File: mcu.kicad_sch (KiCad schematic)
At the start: 41 parts, among them J1 GPIO, J2 3v3/GND, Q1 MMBTA42, U1 STM32F103C8Tx, X1 SPI_DBG, X2 MTRBTN, X3 Bluetooth, X4 Buzzer

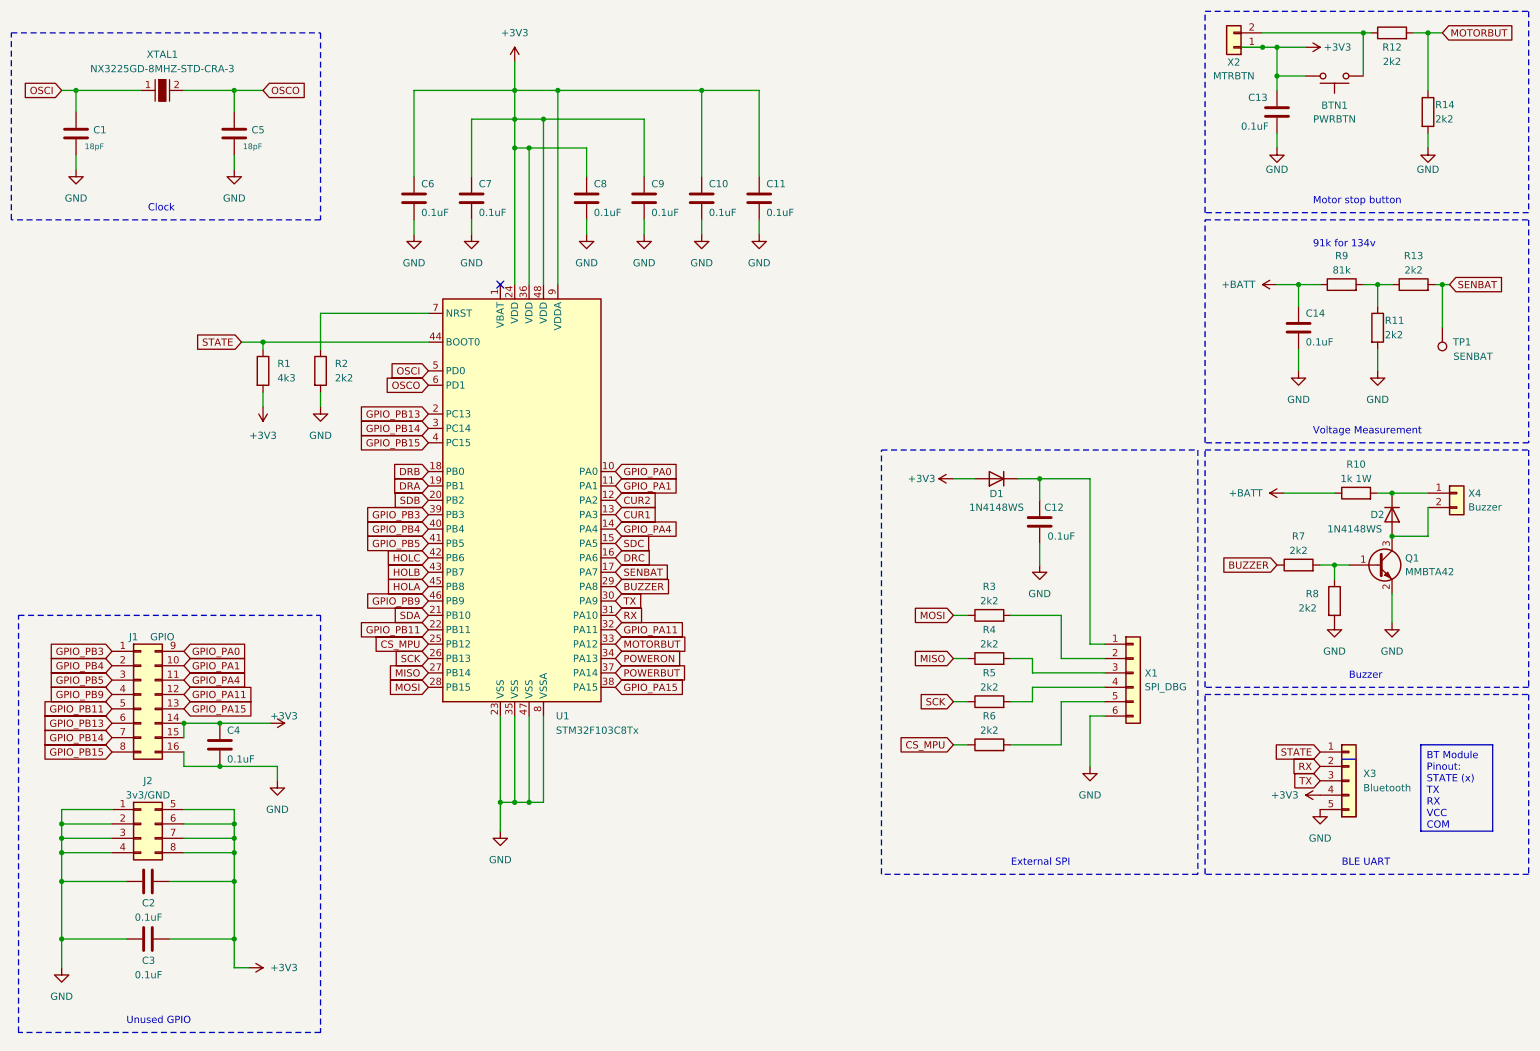
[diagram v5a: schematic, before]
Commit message: Add files via upload
Add leds and minors
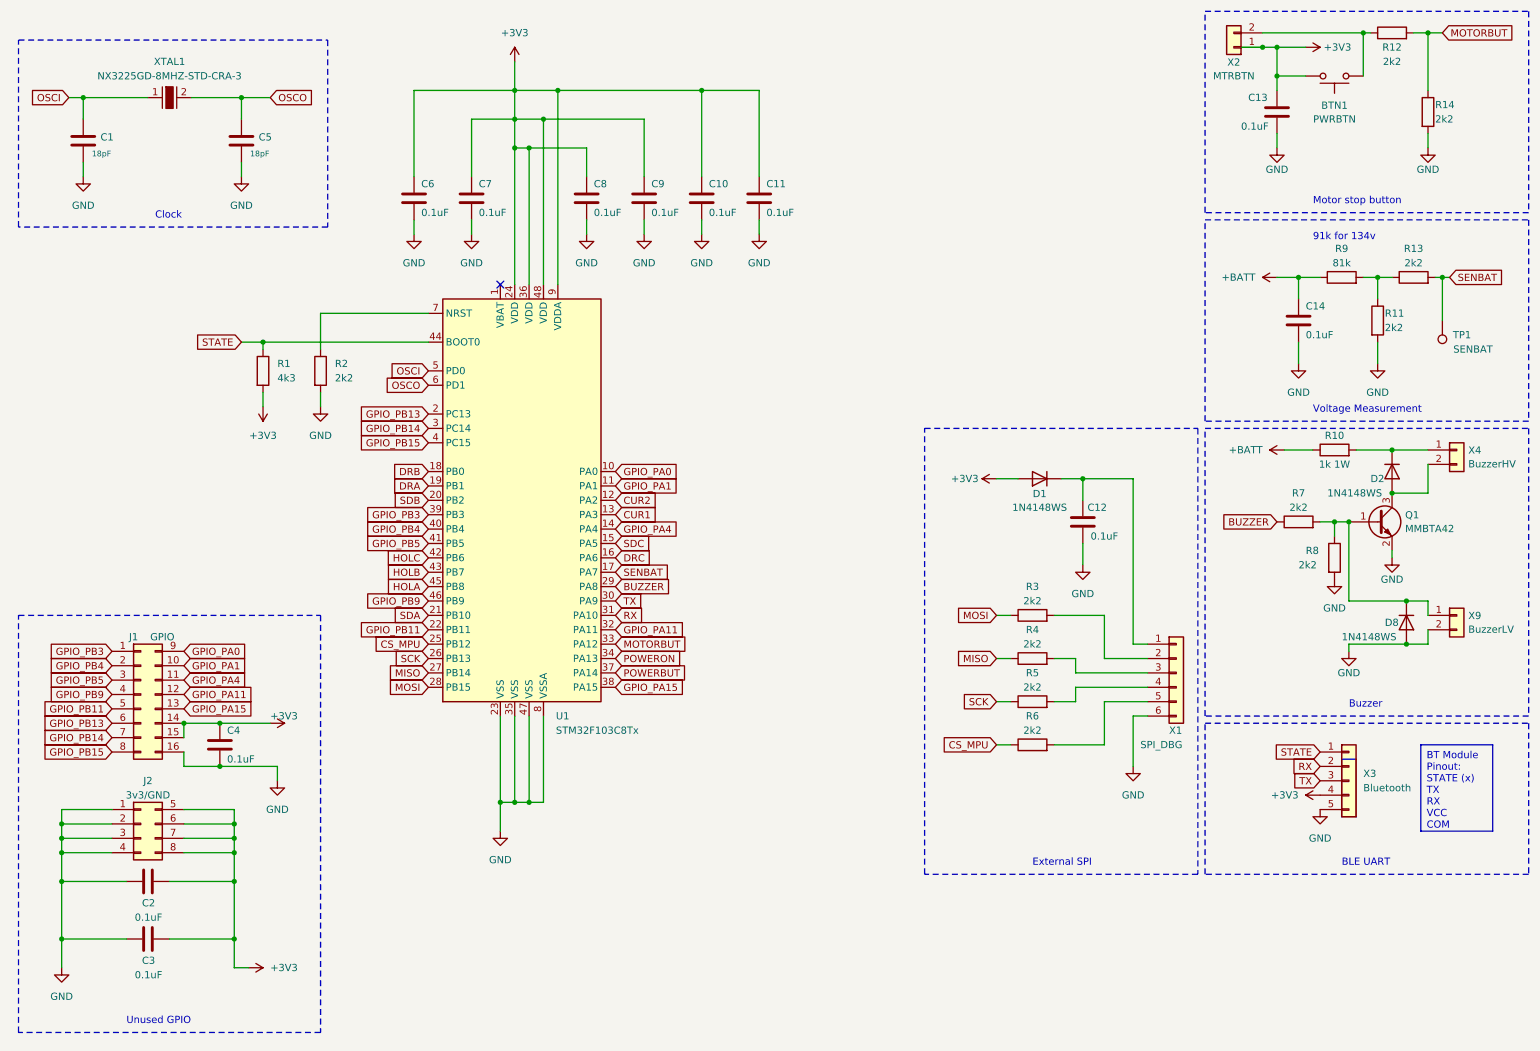
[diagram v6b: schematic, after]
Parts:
- added D8: 1N4148WS, Diode_SMD:D_SOD-323, symbol Diode:1N4148WS
- added X9: BuzzerLV, symbol Connector_Generic:Conn_01x02
- X4: value Buzzer -> BuzzerHV
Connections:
- net GND: now also D8.2 (A), X9.2 (Pin_2)
- net at Q1.1 (B), R7.2, R8.1: now also D8.1 (K), X9.1 (Pin_1)
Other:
- moved on the sheet: C1, C12, C14, C5, D1, D2, Q1, R10, R11, R13, R3, R4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

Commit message: fixed some footprints
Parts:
- J1: footprint Capacitor_SMD:CP_Elec_10x10.5 -> Connector_PinSocket_2.54mm:PinSocket_2x08_P2.54mm_Vertical
- J2: footprint Capacitor_SMD:CP_Elec_6.3x7.7 -> Connector_PinSocket_2.54mm:PinSocket_2x04_P2.54mm_Vertical
- R10: renamed from R9; value 81k -> 81k 1%; footprint Resistor_SMD:R_0603_1608Metric_Pad0.98x0.95mm_HandSolder -> Resistor_SMD:R_0805_2012Metric_Pad1.20x1.40mm_HandSolder
- R11: value 2k2 -> 2k2 1%; footprint Resistor_SMD:R_0603_1608Metric_Pad0.98x0.95mm_HandSolder -> Resistor_SMD:R_0805_2012Metric_Pad1.20x1.40mm_HandSolder
- renumbered D8 to D3, R10 to R8, R8 to R9, X9 to X5

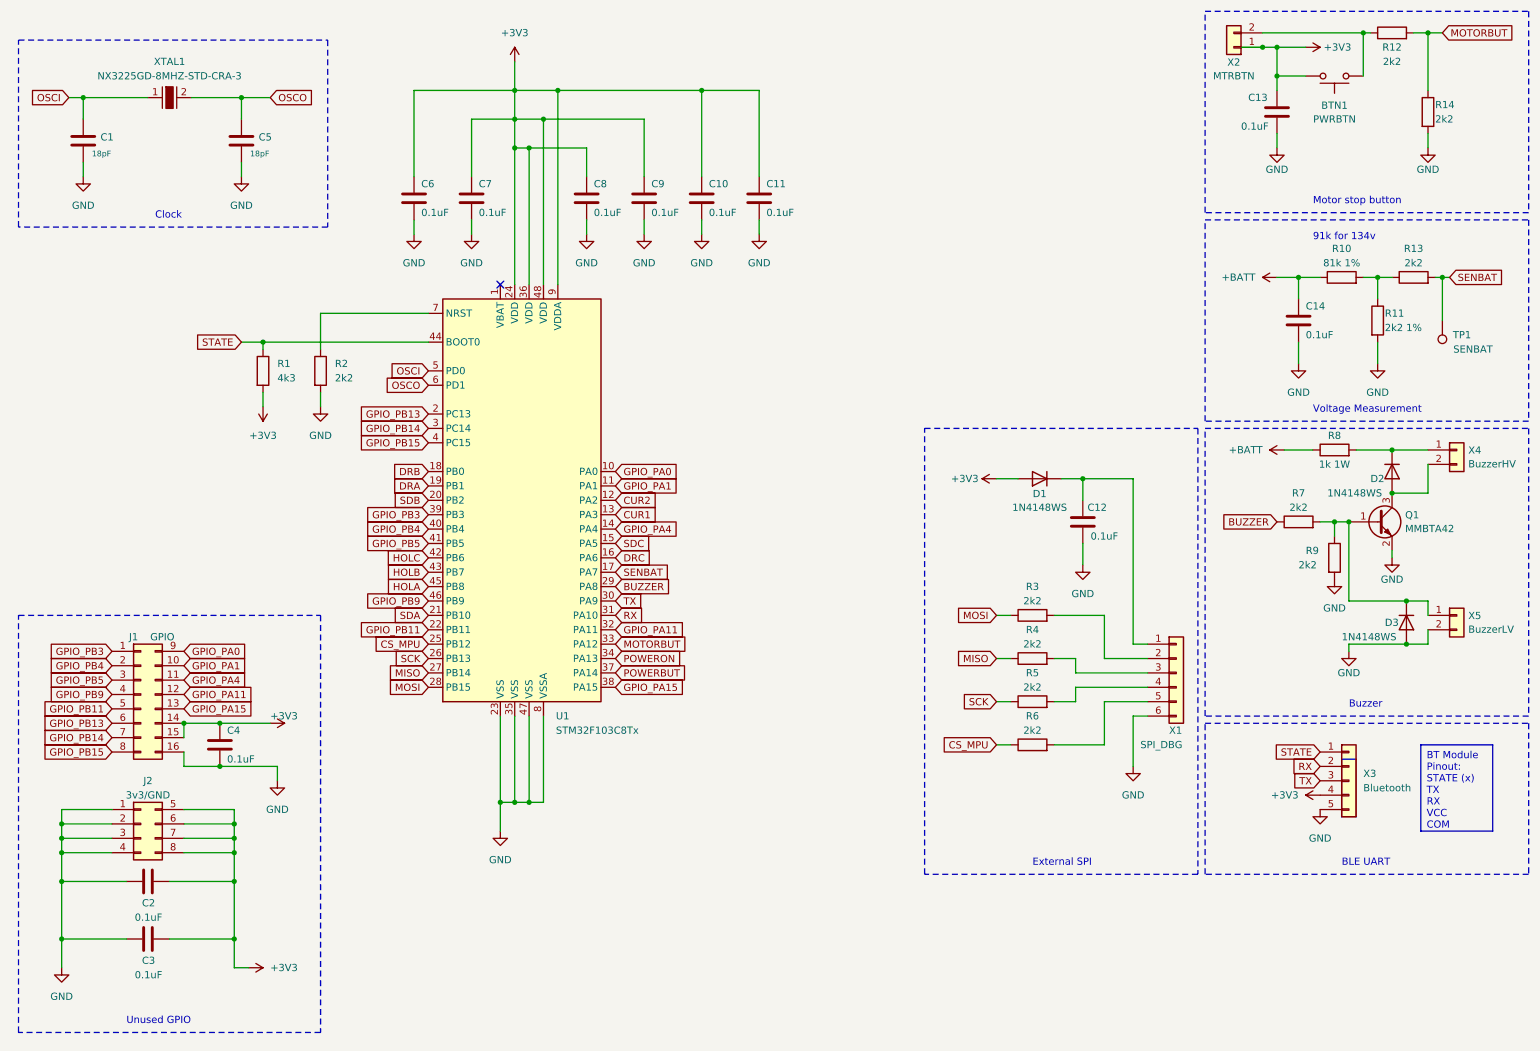
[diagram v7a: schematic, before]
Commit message: Fixed short cirquit, minors
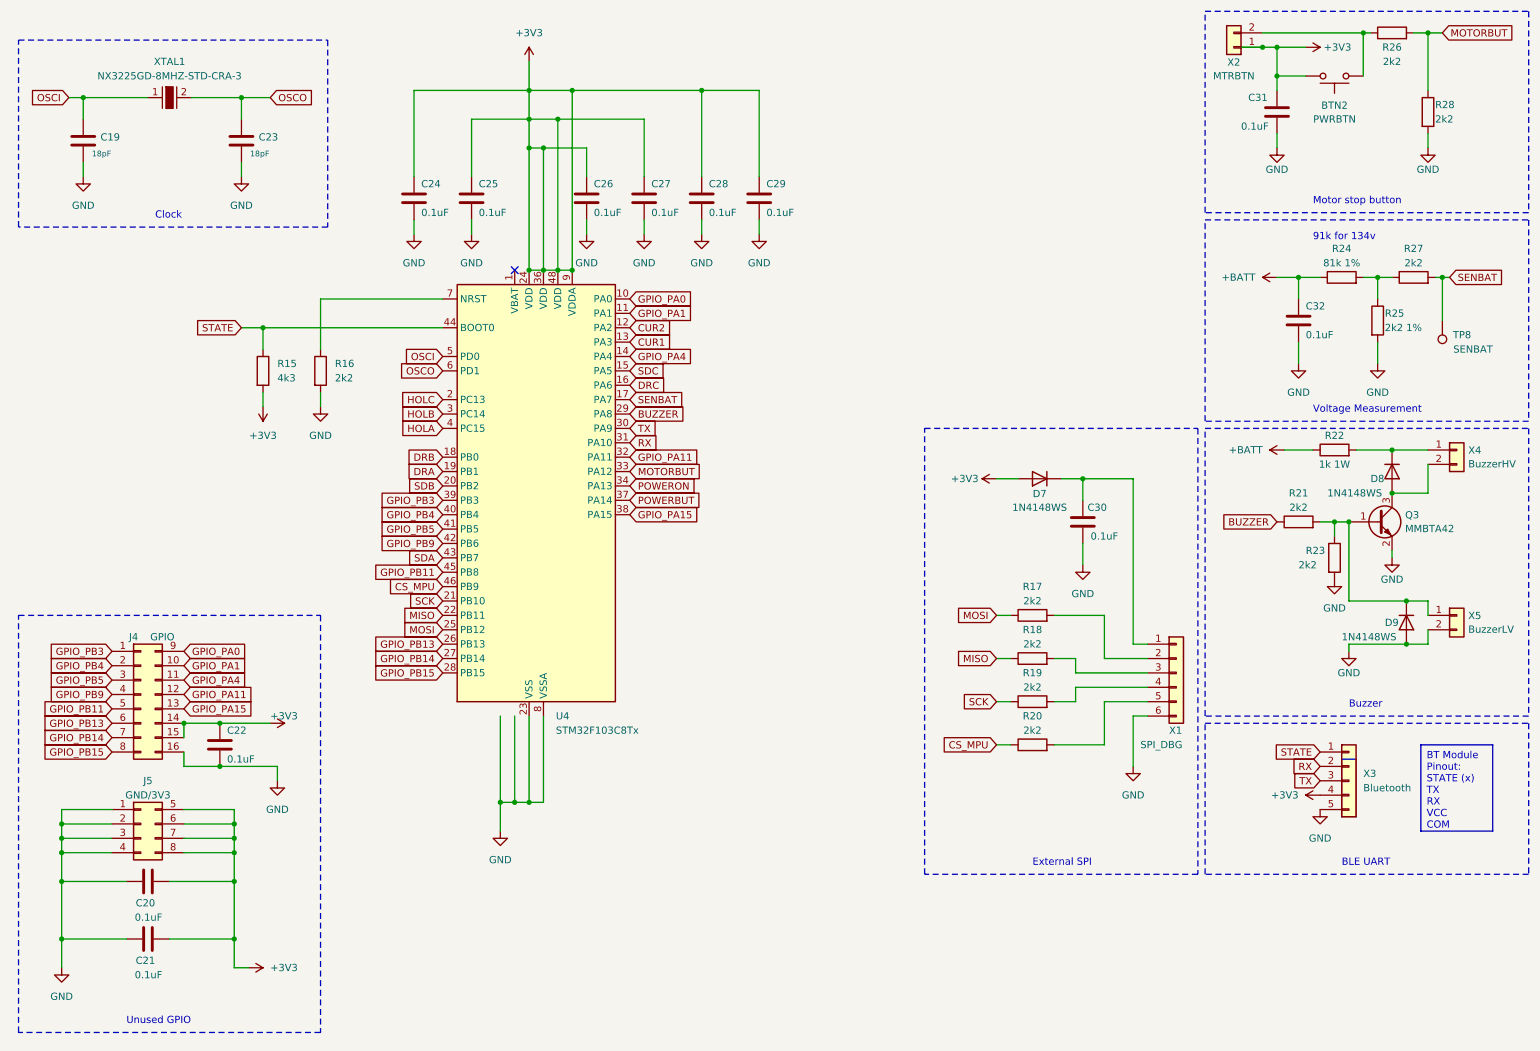
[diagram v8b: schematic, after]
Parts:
- J5: renamed from J2; value 3v3/GND -> GND/3V3
- renumbered BTN1 to BTN2, C1 to C19, C2 to C20, C3 to C21, C4 to C22, C5 to C23, C6 to C24, C7 to C25, C8 to C26, C9 to C27, C10 to C28, C11 to C29, C12 to C30, C13 to C31, C14 to C32, D1 to D7, D2 to D8, D3 to D9, J1 to J4, Q1 to Q3, R1 to R15, R2 to R16, R3 to R17, R4 to R18, R5 to R19, R6 to R20, R7 to R21, R8 to R22, R9 to R23, R10 to R24, R11 to R25, R12 to R26, R13 to R27, R14 to R28, TP1 to TP8, U1 to U4
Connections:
- net CS_MPU: now also U4.46 (PB9); no longer U4.25 (PB12)
- net GPIO_PB11: now also U4.45 (PB8); no longer U4.22 (PB11)
- net GPIO_PB13: now also U4.26 (PB13); no longer U4.2 (PC13)
- net GPIO_PB14: now also U4.27 (PB14); no longer U4.3 (PC14)
- net GPIO_PB15: now also U4.28 (PB15); no longer U4.4 (PC15)
- net GPIO_PB9: now also U4.42 (PB6); no longer U4.46 (PB9)
- net HOLA: now also U4.4 (PC15); no longer U4.45 (PB8)
- net HOLB: now also U4.3 (PC14); no longer U4.43 (PB7)
- net HOLC: now also U4.2 (PC13); no longer U4.42 (PB6)
- net MISO: now also U4.22 (PB11); no longer U4.27 (PB14)
- net MOSI: now also U4.25 (PB12); no longer U4.28 (PB15)
- net SCK: now also U4.21 (PB10); no longer U4.26 (PB13)
- net SDA: now also U4.43 (PB7); no longer U4.21 (PB10)
